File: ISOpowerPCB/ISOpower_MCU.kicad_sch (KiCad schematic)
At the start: 24 parts

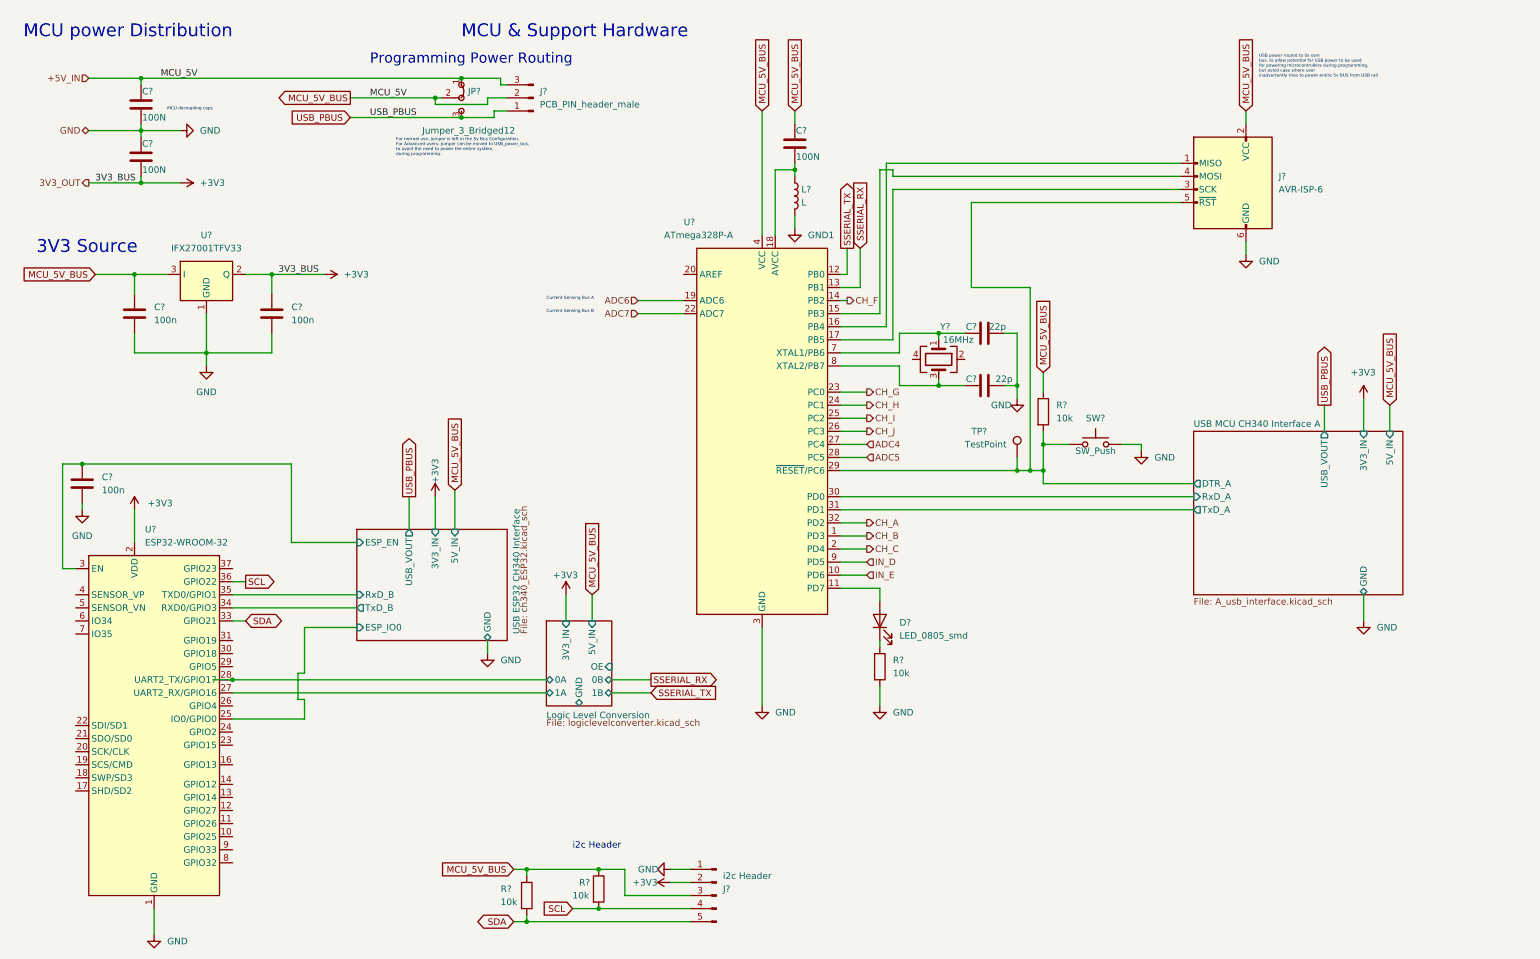
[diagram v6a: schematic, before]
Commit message: Updated as per discussions 26/01/22
# Change Notes

04/02/2022
As per discussion 26/01/22
1. Changed per channel 5v MOSFET switches to MOSFET control of DC/DC module on/off pin - due to failure of MOSFET switching during testing.
2. Added 5v buck converter for independent MCU_5V power bus.
	- Ensured all 5v MCU hardware is powered from common MCU_5V bus.
3. Removed circuit from NC pins on DC/DC modules.
4. Changed ESP32 USB interface to CH340
5. Changed MCU serial logic level converters from MOSFET to IC - TXS0102DCT
	- TODO: OE pin now requires low signal untill DC/DC supply is stable - Does it? Can it just be tied to 5v bus with a large capacitor? Does it need MCU to hold pin low untill 5V_BUS is stable?
6. Removed redundent 3V3_IN to power distribution page.
	- Rechecked all sheets for redundent pins, it won't impact drawing traces, but it will impact readability.
7. Added Mechanical layer as hirarchical sheet.
8. Moved voltage monitoring circuits to hirarchical sheet
9. Added voltage monitoring with TL431DBZ to 12V_BUS
10. Automatic shutoff circuit removed, as this would prevent the DC/DC module from powering on. Instead moved to AtMega328p digital inputs
and microcontroller will control shutdown of DC/DC supply if out of spec voltage detected.
		- This is a severe limitation compared to the specification, and this also does not prevent damage to devices on 5V_BUS if voltage is pulled high, for example to 12v due to user error.
		- TODO: Add independent overvoltage protection to 5V_BUS? 		[Zener Diode Overvoltage Protection - Sparkfun](https://www.rs-online.com/designspark/how-does-zener-diode-do-overvoltage-protection-in-circuit#:~:text=In%20order%20to%20protect%20the,flow%20in%20the%20reverse%20direction).
11. Changed logic level conversion for 12v outputs to 12v drive circuit. [12v drive circuit](https://forum.arduino.cc/t/easiest-way-of-driving-amplifying-from-5v-to-12v/123290)
12. Added proto pin connections for ESP MCU.
13. Changed 20v Zener in reverse vol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
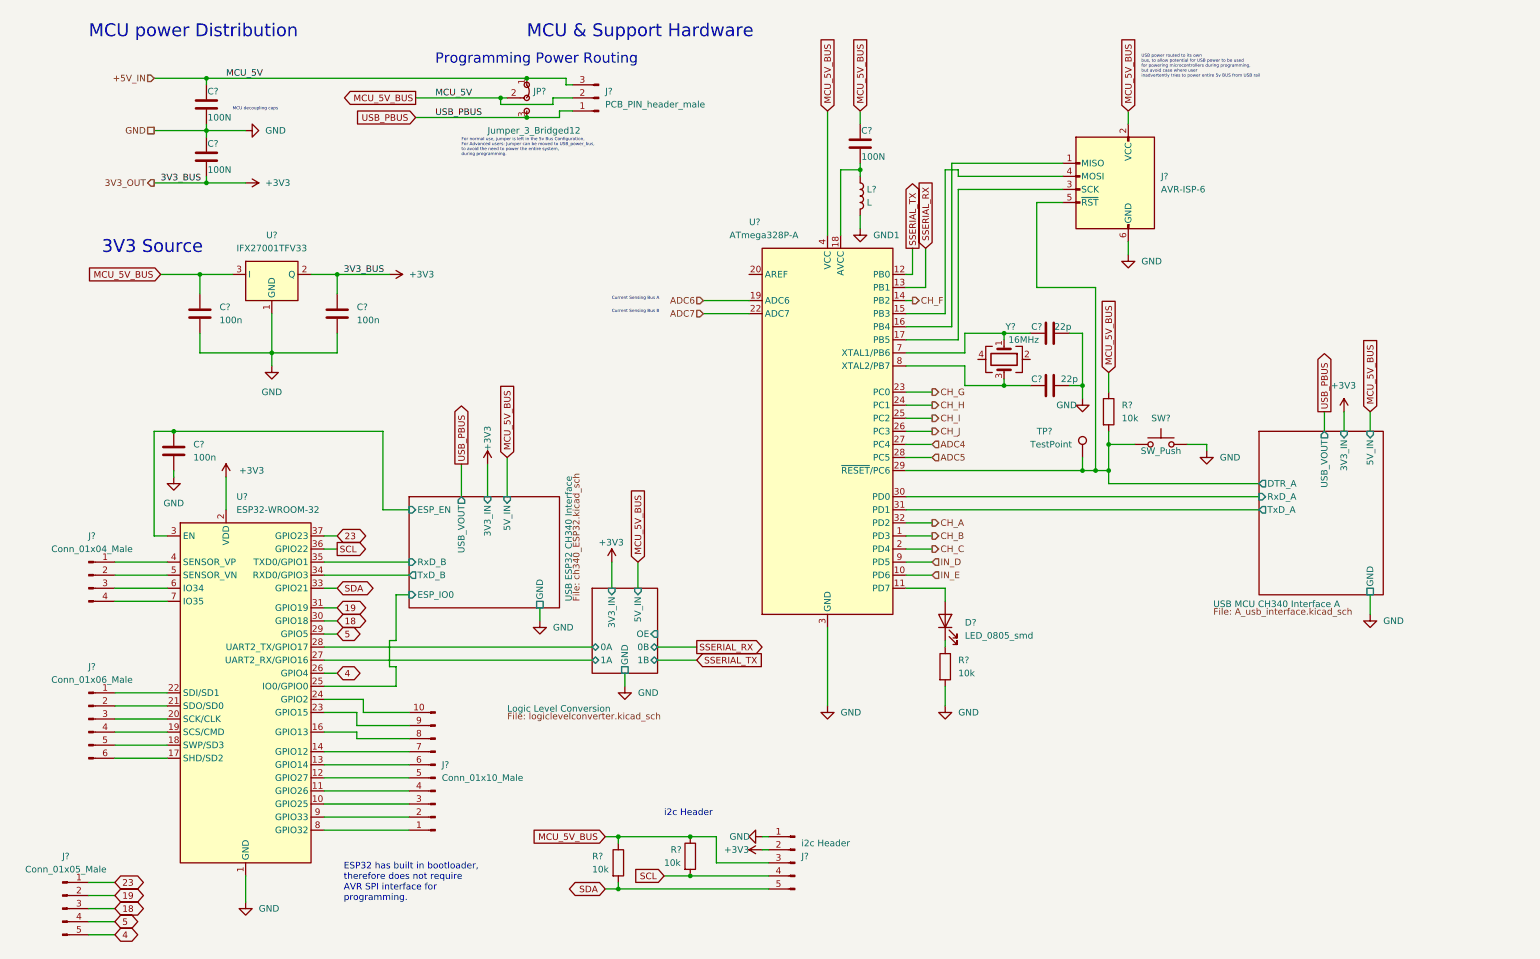
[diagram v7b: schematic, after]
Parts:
- added J?: Conn_01x06_Male, symbol Connector:Conn_01x06_Male
- added J?: Conn_01x10_Male, symbol Connector:Conn_01x10_Male
- added J?: Conn_01x05_Male, symbol Connector:Conn_01x05_Male
- added J?: Conn_01x04_Male, symbol Connector:Conn_01x04_Male
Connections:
- net at U?.10 (GPIO25): now also J?.3 (Pin_3)
- net at U?.11 (GPIO26): now also J?.4 (Pin_4)
- net at U?.12 (GPIO27): now also J?.5 (Pin_5)
- net at U?.13 (GPIO14): now also J?.6 (Pin_6)
- net at U?.14 (GPIO12): now also J?.7 (Pin_7)
- net at U?.16 (GPIO13): now also J?.8 (Pin_8)
- net at U?.17 (SHD/SD2): now also J?.6 (Pin_6)
- net at U?.18 (SWP/SD3): now also J?.5 (Pin_5)
- net at U?.19 (SCS/CMD): now also J?.4 (Pin_4)
- net at U?.20 (SCK/CLK): now also J?.3 (Pin_3)
- net at U?.21 (SDO/SD0): now also J?.2 (Pin_2)
- net at U?.22 (SDI/SD1): now also J?.1 (Pin_1)
- net at U?.23 (GPIO15): now also J?.9 (Pin_9)
- net at U?.24 (GPIO2): now also J?.10 (Pin_10)
- net 4: now reaches U?.26 (GPIO4)
- net 4: now also J?.5 (Pin_5)
- net 5: now reaches U?.29 (GPIO5)
- net 5: now also J?.4 (Pin_4)
- net 18: now reaches U?.30 (GPIO18)
- net 18: now also J?.3 (Pin_3)
- net 19: now reaches U?.31 (GPIO19)
- net 19: now also J?.2 (Pin_2)
- net 23: now reaches U?.37 (GPIO23)
- net 23: now also J?.1 (Pin_1)
- net at U?.4 (SENSOR_VP): now also J?.1 (Pin_1)
- net at U?.5 (SENSOR_VN): now also J?.2 (Pin_2)
- net at U?.6 (IO34): now also J?.3 (Pin_3)
- net at U?.7 (IO35): now also J?.4 (Pin_4)
- net at U?.8 (GPIO32): now also J?.1 (Pin_1)
- net at U?.9 (GPIO33): now also J?.2 (Pin_2)
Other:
- note added: "ESP32 has built in bootloader, therefore does not require AVR SPI interface for programming."
- moved on the sheet: C?, D?, J?, JP?, L?, R?, SW?, TP?, U?, Y?

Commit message: messing around with libraries
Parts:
- C1, C2, C3, C4, C5, C6, C7, C8: renamed from C?; symbol 000_Capacitor_film_immo:cap_film_0805 -> 000_Capacitor_FIlm_Immo:cap_film_0805
- gave numbers to parts that had none: 20
